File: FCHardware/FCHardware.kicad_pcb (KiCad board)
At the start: 2 copper layers, 39 x 39 mm, 51 parts, among them J2 JST-4pin, J3 JST-8pin, J4 UJ20-C-H-G-SMT-2A-P16-TR, U1 ICM-42688-P, U2 STM32F405RGTx, U3 USBLC6-2SC6, U4 AP2112K-3.3, U5 TPSM63603

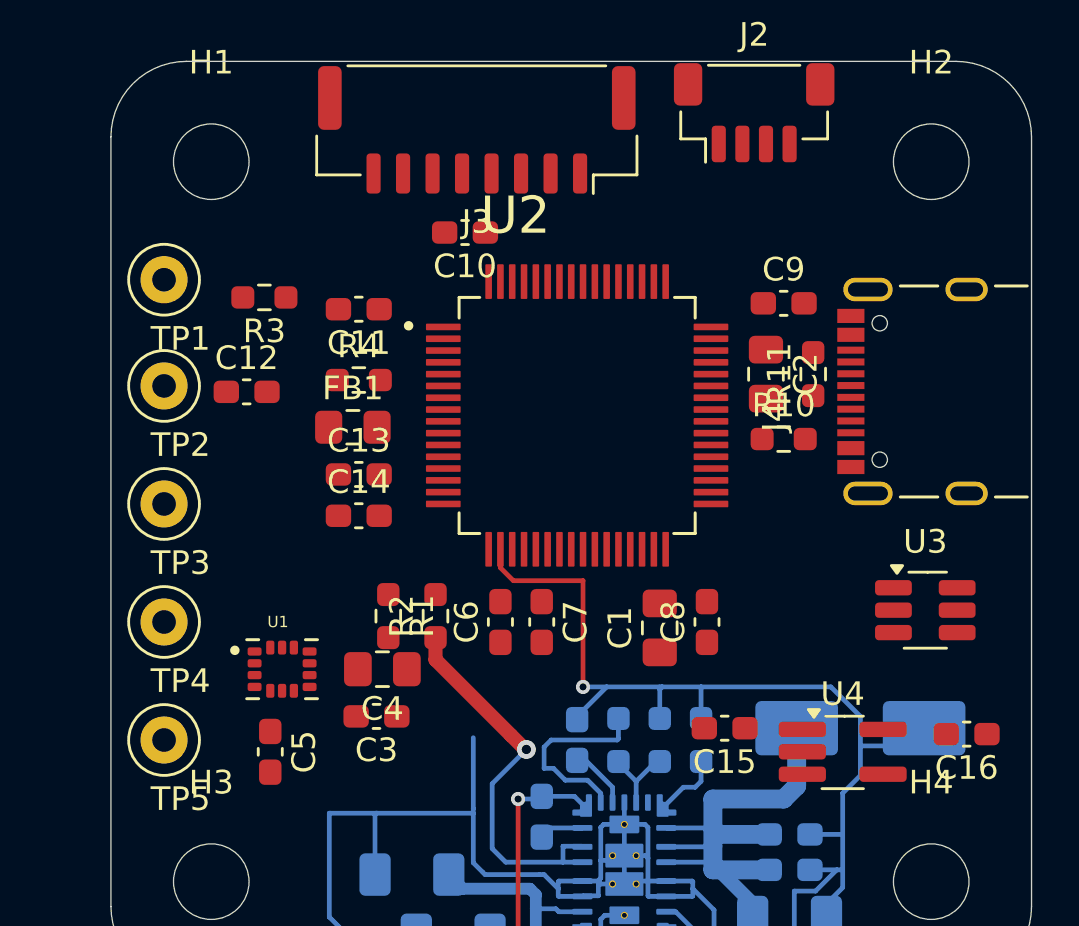
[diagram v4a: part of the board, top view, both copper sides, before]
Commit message: Swiched schematics for easier routing, provisional routing of STM32
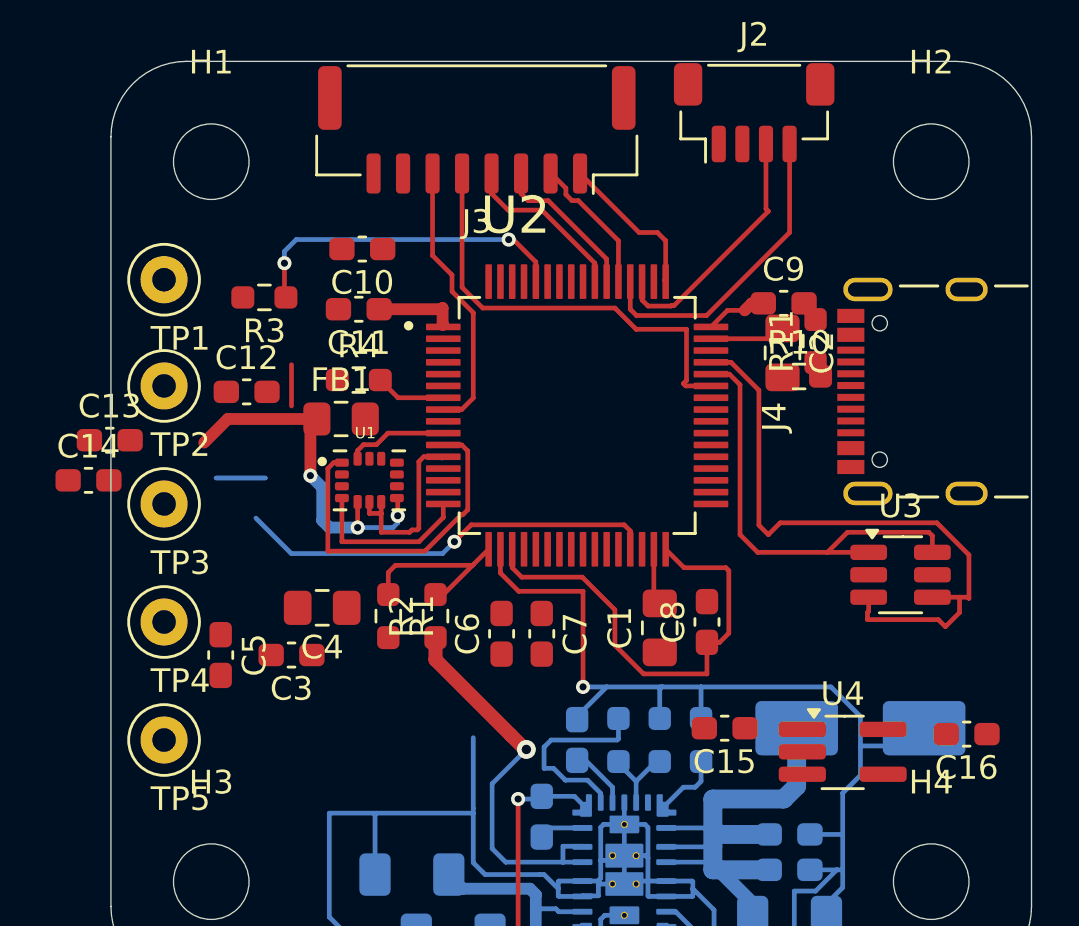
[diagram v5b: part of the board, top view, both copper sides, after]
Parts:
- moved C14 11.5 mm to (79.3, 98.0)
- moved C13 10.6 mm to (80.2, 96.3)
- moved U1 8.81 mm to (91.2, 98.0)
- moved C5 4.61 mm to (84.9, 105.4)
- moved C3 4.44 mm to (87.9, 105.4)
- moved C10 4.41 mm to (90.9, 88.2)
- moved C4 3.64 mm to (89.2, 103.4)
- moved R10 2.73 mm to (109.4, 93.6)
- moved U3 1.83 mm to (113.7, 102.0)
- moved R11 1.40 mm to (110.1, 92.1)
- moved C2 1.14 mm to (108.7, 92.6)
- moved FB1 0.61 mm to (90.0, 95.4)
- moved C6 0.50 mm to (96.8, 104.5)
- moved C7 0.50 mm to (98.5, 104.5)
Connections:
- J2 pad 3: /RC_TX -> /RC_RX
- J2 pad 4: /RC_RX -> /RC_TX
- J3 pad 1: /ESC_TELE -> /M1
- J3 pad 2: /ESC_CRT -> /M2
- J3 pad 3: /M1 -> /M3
- J3 pad 4: /M2 -> /M4
- J3 pad 5: /M3 -> /ESC_TELE
- J3 pad 6: /M4 -> /ESC_CRT
- U2 pad 10: unconnected-(U2-PC2-Pad10) -> /IMU_SDI
- U2 pad 11: unconnected-(U2-PC3-Pad11) -> /IMU_SDO
- U2 pad 15: /ESC_CRT -> unconnected-(U2-PA1-Pad15)
- U2 pad 16: unconnected-(U2-PA2-Pad16) -> /IMU_INT
- U2 pad 21: /M1 -> /IMU_CS
- U2 pad 22: /M2 -> unconnected-(U2-PA6-Pad22)
- U2 pad 23: /M3 -> unconnected-(U2-PA7-Pad23)
- U2 pad 26: /IMU_INT -> unconnected-(U2-PB0-Pad26)
- U2 pad 27: /IMU_CS -> unconnected-(U2-PB1-Pad27)
- U2 pad 29: /RC_RX -> /IMU_SCLK
- U2 pad 30: /RC_TX -> unconnected-(U2-PB11-Pad30)
- U2 pad 41: /M4 -> unconnected-(U2-PA8-Pad41)
- U2 pad 49: unconnected-(U2-PA14-Pad49) -> /M1
- U2 pad 51: unconnected-(U2-PC10-Pad51) -> /RC_RX
- U2 pad 52: unconnected-(U2-PC11-Pad52) -> /RC_TX
- U2 pad 53: unconnected-(U2-PC12-Pad53) -> /M2
- U2 pad 54: unconnected-(U2-PD2-Pad54) -> /M3
- U2 pad 55: unconnected-(U2-PB3-Pad55) -> /M4
- U2 pad 56: /IMU_SDI -> unconnected-(U2-PB4-Pad56)
- U2 pad 57: /IMU_SDO -> unconnected-(U2-PB5-Pad57)
- U2 pad 58: /IMU_SCLK -> unconnected-(U2-PB6-Pad58)
- U2 pad 8: unconnected-(U2-PC0-Pad8) -> /ESC_CRT
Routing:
- net +3V3: track 0.00 -> 41.3 mm, vias 0 -> 3
- net /USB_D+: track 0.00 -> 27.4 mm
- net /USB_D-: track 0.00 -> 19.1 mm
- net /ESC_TELE: track 0.00 -> 18.8 mm
- net /IMU_SCLK: track 0.00 -> 18.1 mm, vias 0 -> 1
- net /IMU_SDO: track 0.00 -> 16.6 mm
- net /BOOT0: track 0.00 -> 14.1 mm, vias 0 -> 2
- net /RC_TX: track 0.00 -> 13.2 mm
- net /ESC_CRT: track 0.00 -> 11.7 mm
- net /RC_RX: track 0.00 -> 10.8 mm
- net GND: track 102.4 -> 110.2 mm
- net /M4: track 0.00 -> 7.75 mm
- net /V_MON: track 0.00 -> 7.70 mm
- net /IMU_INT: track 0.00 -> 7.14 mm
- net /M1: track 0.00 -> 6.62 mm
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
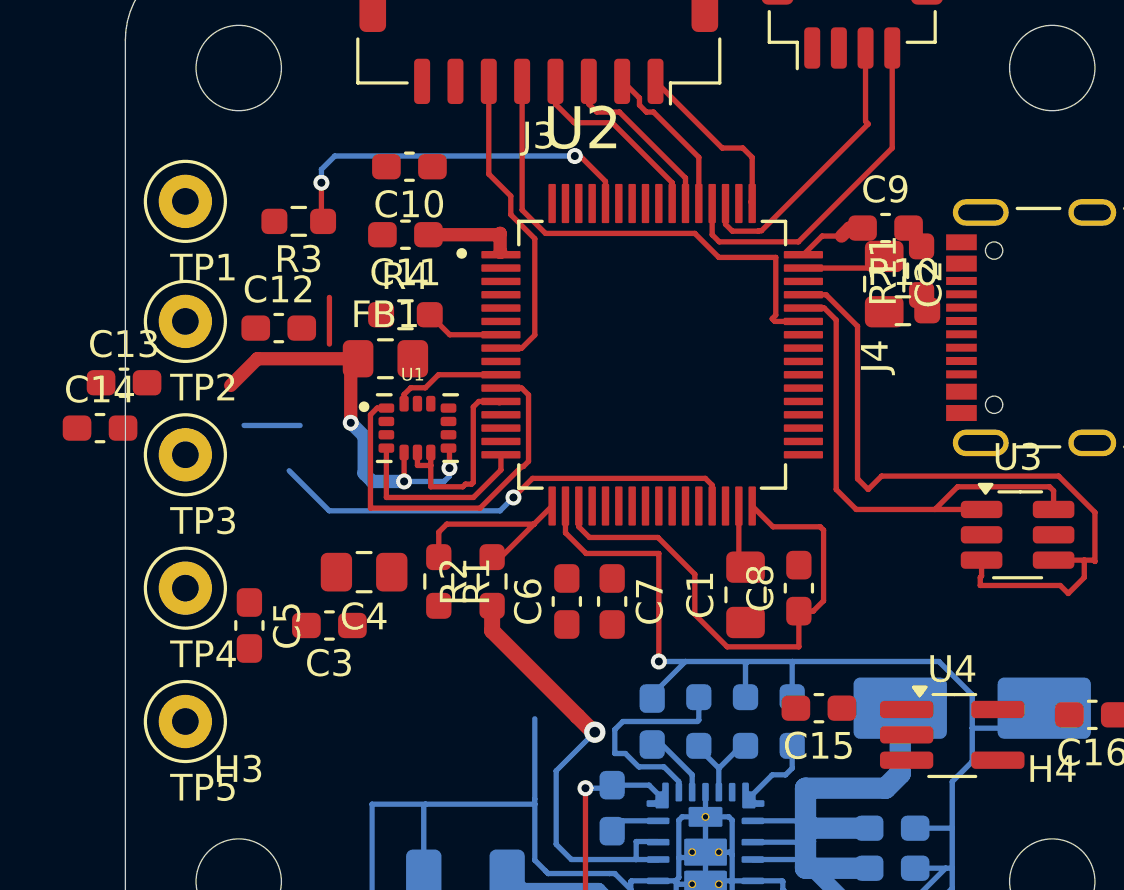
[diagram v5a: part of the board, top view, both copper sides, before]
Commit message: Routed MCU's Capacitors and Resistors Inputs
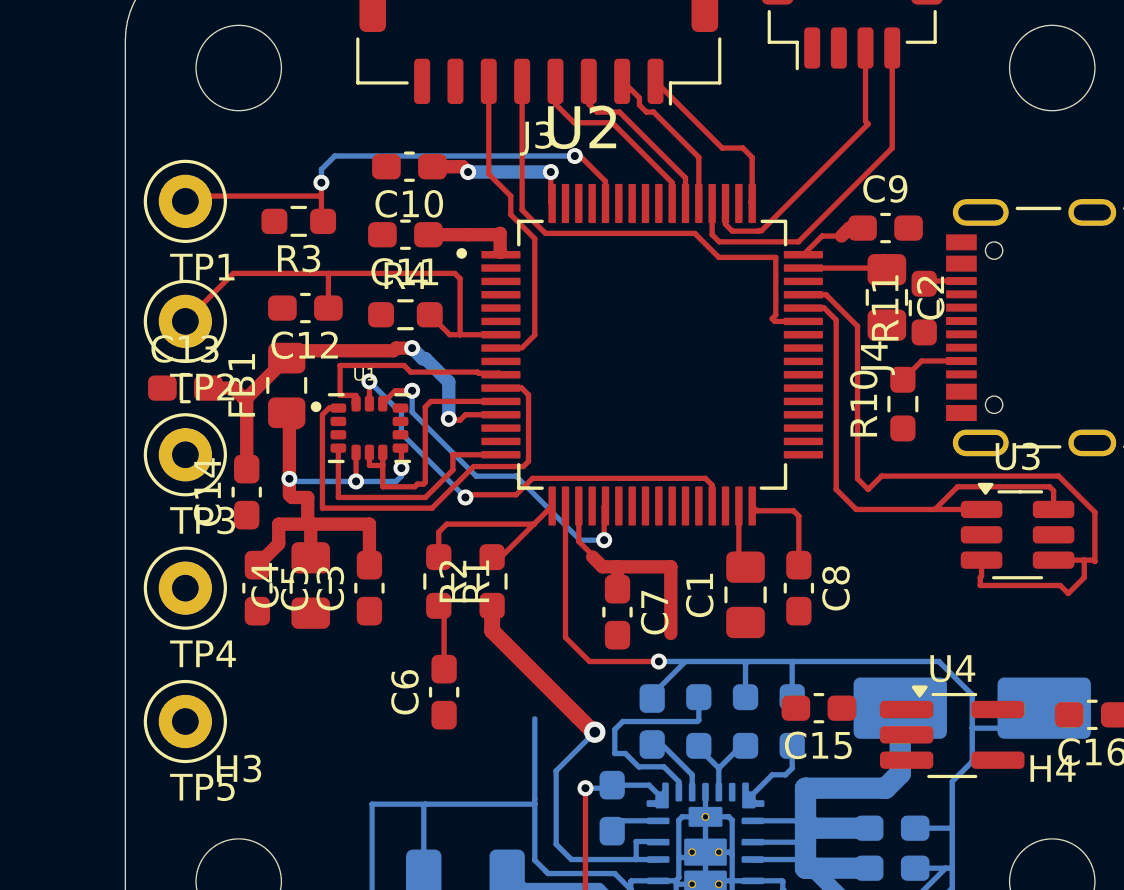
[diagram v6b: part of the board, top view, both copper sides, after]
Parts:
- moved C14 6.00 mm to (84.8, 100.4), turned to 90 degrees
- moved C6 5.72 mm to (92.2, 107.9)
- moved FB1 3.83 mm to (86.3, 96.4), turned to 90 degrees
- moved R10 3.50 mm to (109.4, 97.1), turned to 90 degrees
- moved C13 2.31 mm to (82.5, 96.5)
- moved C4 2.06 mm to (87.2, 103.9), turned to 90 degrees
- moved C3 2.05 mm to (89.4, 104.0), turned to 90 degrees
- moved U1 1.80 mm to (89.4, 98.0)
- moved C5 1.43 mm to (85.2, 104.0)
- moved R11 1.40 mm to (110.2, 93.5)
- moved C12 1.25 mm to (87.0, 93.5), turned to 180 degrees
- moved C2 0.51 mm to (108.8, 93.1)
- moved C7 0.45 mm to (98.7, 104.9)
- turned C8 to -90 degrees
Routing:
- net /VDD33A: track 0.00 -> 16.6 mm, vias 0 -> 2
- net /NRST: track 2.98 -> 17.5 mm
- net /IMU_CS: track 0.00 -> 12.6 mm, vias 0 -> 2
- net /BOOT0: track 14.1 -> 19.2 mm
- net /IMU_SDI: track 4.28 -> 8.35 mm
- net +3V3: track 41.3 -> 44.0 mm, vias 3 -> 5
- net Net-(J4-CC1): track 0.00 -> 2.49 mm
- net Net-(C6-Pad2): track 0.00 -> 2.46 mm
- net /IMU_INT: track 7.14 -> 8.94 mm
- net (no net): track 1.75 -> 0.00 mm
- net GND: track 110.2 -> 111.8 mm
- net Net-(J4-CC2): track 0.00 -> 1.44 mm
- net /IMU_SCLK: track 18.1 -> 17.3 mm, vias 1 -> 2
- net /ESC_CRT: track 11.7 -> 10.9 mm

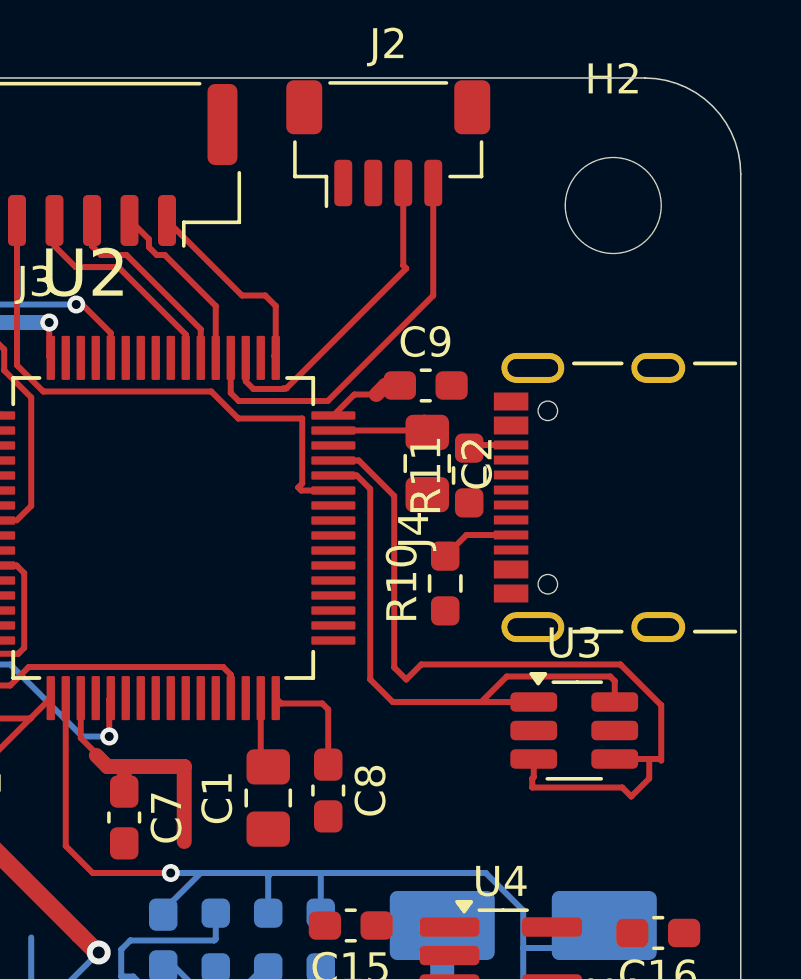
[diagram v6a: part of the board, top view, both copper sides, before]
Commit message: Wired the USB C
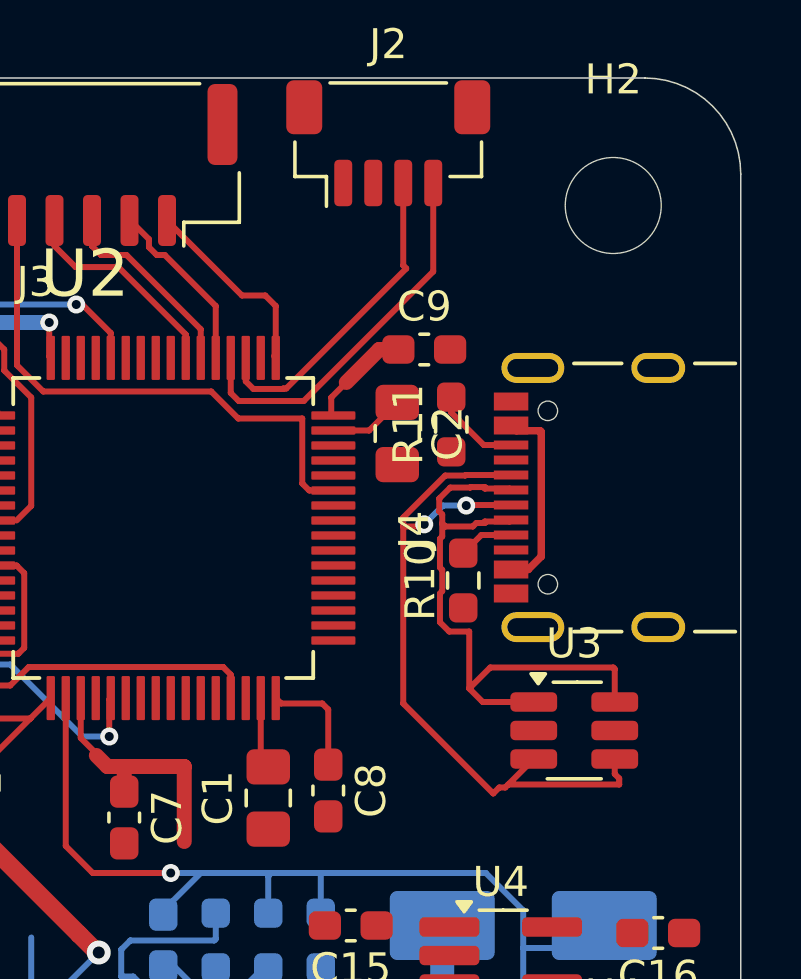
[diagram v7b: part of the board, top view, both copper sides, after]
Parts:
- moved R11 1.80 mm to (109.6, 91.8)
- moved C2 1.41 mm to (107.8, 92.1)
- moved C9 1.20 mm to (108.7, 89.3)
- moved R10 0.61 mm to (110.0, 97.0)
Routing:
- net USB_VBUS: track 0.00 -> 6.43 mm
- net /USB_D+: track 27.4 -> 25.0 mm, vias 0 -> 2
- net /USB_D-: track 19.1 -> 21.0 mm
- net Net-(J4-CC2): track 1.44 -> 2.96 mm
- net +3V3: track 44.0 -> 44.9 mm
- net Net-(U2-VCAP_2): track 3.21 -> 2.52 mm
- net Net-(J4-CC1): track 2.49 -> 1.84 mm

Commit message: Fixed USB C routing
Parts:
- R10, R11, R2, R3, R4: moved to B.Cu
- R8, R9: moved to F.Cu
- moved C6 4.12 mm to (93.2, 103.9)
- moved R3 3.29 mm to (90.0, 90.8)
- moved R1 3.00 mm to (95.0, 103.9), turned to 90 degrees
- moved R4 2.36 mm to (88.4, 93.5)
- moved R10 1.93 mm to (108.1, 97.3)
- moved C9 1.82 mm to (110.1, 88.1)
- moved D1 1.80 mm to (110.2, 108.6)
- moved R7 1.75 mm to (103.5, 109.0)
- moved R11 1.66 mm to (108.1, 92.5)
- moved C16 1.58 mm to (116.8, 107.2), turned to -90 degrees
- moved U4 1.35 mm to (112.6, 109.4)
- moved C20 1.30 mm to (101.3, 109.0)
- moved R2 1.01 mm to (95.0, 103.9)
- moved C2 0.90 mm to (108.5, 91.5)
- moved R8 0.45 mm to (101.3, 109.0)
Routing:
- net +5V: track 37.9 -> 70.0 mm, vias 0 -> 2
- net VBAT: track 39.5 -> 66.7 mm
- net GND: track 111.8 -> 123.9 mm, vias 1 -> 3
- net +3V3: track 44.9 -> 49.4 mm
- net /NRST: track 17.5 -> 19.6 mm, vias 0 -> 1
- net Net-(J4-CC1): track 1.84 -> 3.87 mm, vias 0 -> 1
- net /V_MON: track 7.70 -> 5.97 mm, vias 0 -> 1
- net Net-(U2-VCAP_2): track 2.52 -> 3.75 mm
- net /BOOT0: track 19.2 -> 20.5 mm
- net /USB_D+: track 25.0 -> 23.9 mm, vias 2 -> 3
- net Net-(U5-RT): track 2.93 -> 2.01 mm
- net Net-(J4-CC2): track 2.96 -> 3.87 mm, vias 0 -> 1
- net Net-(U5-VCC): track 2.62 -> 1.87 mm
- net Net-(C6-Pad2): track 2.46 -> 1.82 mm
- net Net-(U5-FB): track 3.40 -> 3.88 mm, vias 0 -> 1
- added copper zone on B.Cu, net GND
- added copper zone on F.Cu, net GND
